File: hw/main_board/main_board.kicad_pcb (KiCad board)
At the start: 8 copper layers, 100 x 100 mm, 392 parts, among them J1 DDR2_SDRAM_SODIMM, J2 SAMTEC_QTH-090-D, J3 GSG-USB-MICRO-B-SHIELD, J4 CONN_5X2, J5 USB3_MICRO_AB, J6 HIROSE_DM3D, J7 BARREL_JACK, P1 CONN_1, P2 CONN_5X2, P3 CONN_1, Q1 BC857, SW1 SW_PUSH, U1 EP4CE30F29, U10 MIC5207YM5, U11 TPS54218, U12 TPS62420, U13 TPS27081A, U14 MIC5207YM5, U15 TPS27081A, U16 TPS27081A, U17 TPS27081A, U18 74LVC2T45, U19 GSG-IP4220CZ6, U2 TUSB1310A, U20 INV1, U3 LPC11U1X, U4 SI5351C-B, U5 GSG-IP4220CZ6, U6 MIC5207YM5, U7 USB3_ESD_SON50-10, U8 TPS2113A, U9 TPS2065C-2, X1 40M, X2 12M, X3 25M

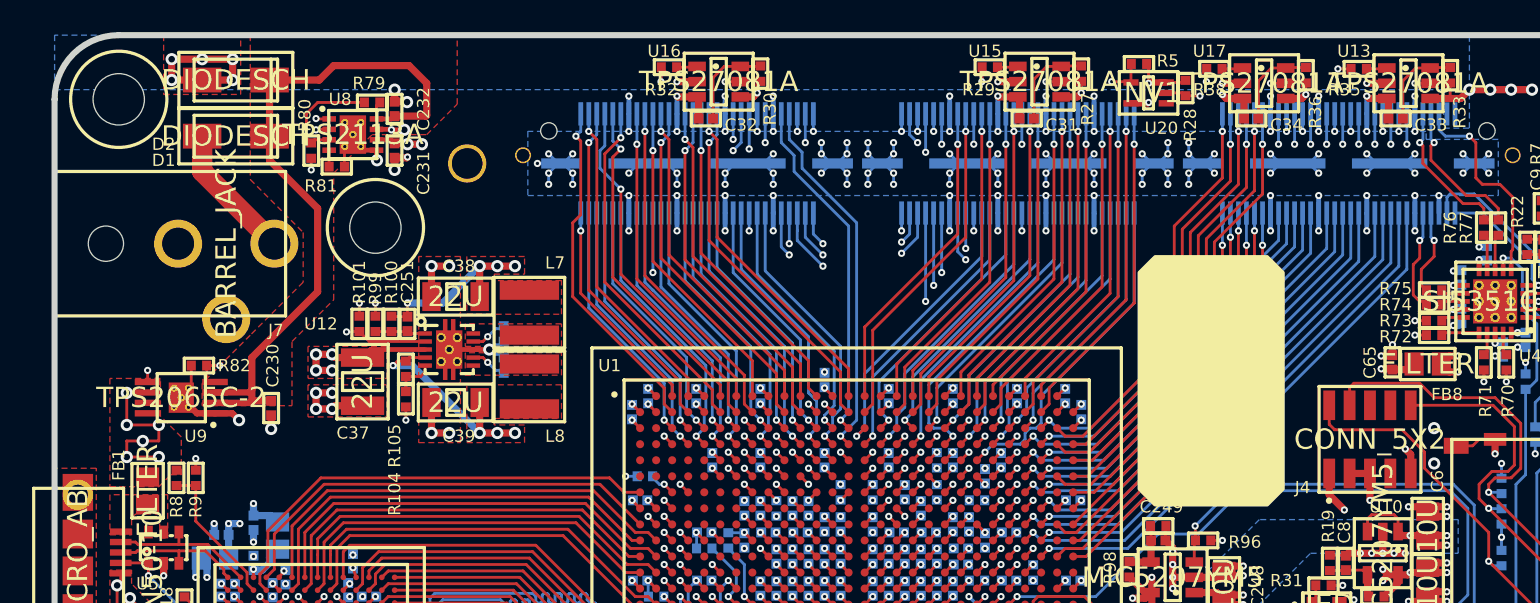
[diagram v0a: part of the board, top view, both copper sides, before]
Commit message: detect front-end module presence by VALT_FE for switching off mainboard IO bank supplies
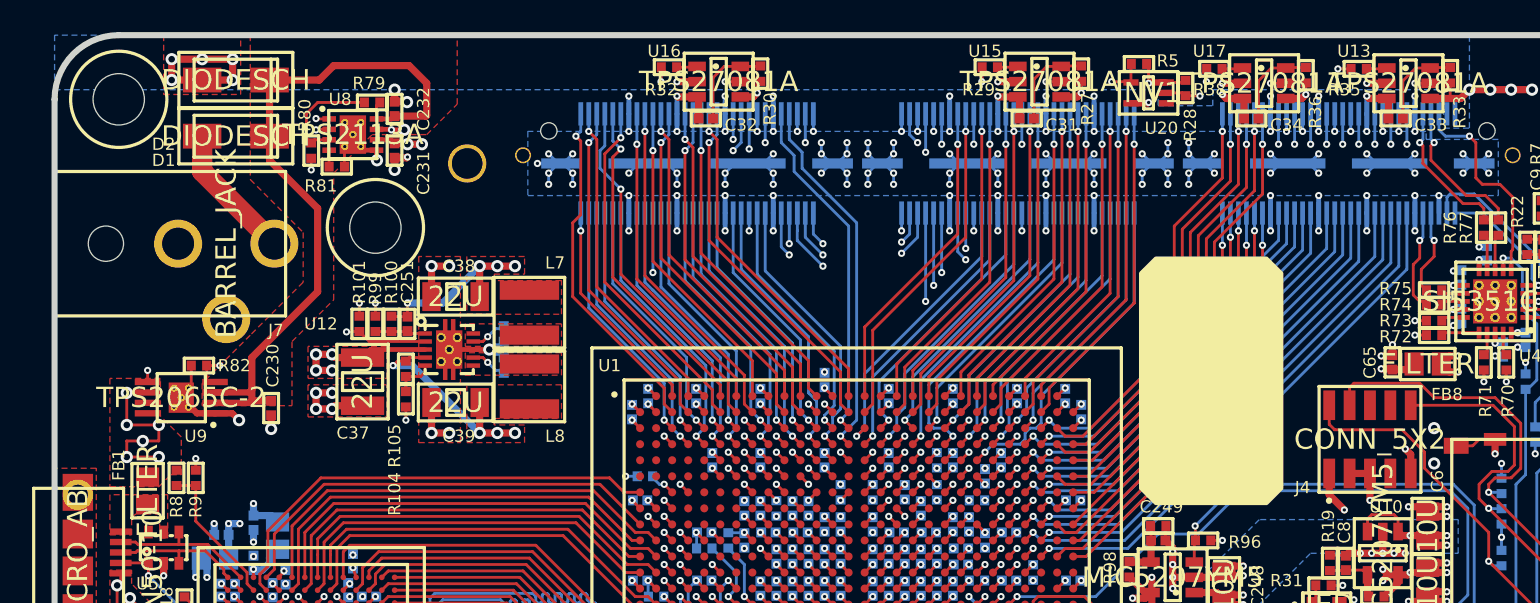
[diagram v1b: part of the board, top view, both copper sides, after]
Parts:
- C8, C9: value 470P -> DNI
- R28: value 10K -> 24K
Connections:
- J1 pad 120: (no net) -> Net-(J1-Pad120)
- J1 pad 163: (no net) -> Net-(J1-Pad163)
- J1 pad 69: (no net) -> Net-(J1-Pad69)
- J1 pad 83: (no net) -> Net-(J1-Pad83)
- J3 pad 4: (no net) -> Net-(J3-Pad4)
- J4 pad 6: (no net) -> Net-(J4-Pad6)
- J4 pad 7: (no net) -> Net-(J4-Pad7)
- J4 pad 8: (no net) -> Net-(J4-Pad8)
- J7 pad 3: (no net) -> Net-(J7-Pad3)
- P2 pad 6: (no net) -> Net-(P2-Pad6)
- P2 pad 7: (no net) -> Net-(P2-Pad7)
- P2 pad 8: (no net) -> Net-(P2-Pad8)
- R28 pad 1: /front_end/FE_EN -> VALT_FE
- U1 pad AA10: (no net) -> Net-(U1-PadAA10)
- U1 pad AA13: (no net) -> Net-(U1-PadAA13)
- U1 pad AA16: (no net) -> Net-(U1-PadAA16)
- U1 pad AA19: (no net) -> Net-(U1-PadAA19)
- U1 pad AA21: (no net) -> Net-(U1-PadAA21)
- U1 pad AA23: (no net) -> Net-(U1-PadAA23)
- U1 pad AA25: (no net) -> Net-(U1-PadAA25)
- U1 pad AA26: (no net) -> Net-(U1-PadAA26)
- U1 pad AA4: (no net) -> Net-(U1-PadAA4)
- U1 pad AA8: (no net) -> Net-(U1-PadAA8)
- U1 pad AB12: (no net) -> Net-(U1-PadAB12)
- U1 pad AB14: (no net) -> Net-(U1-PadAB14)
- U1 pad AB18: (no net) -> Net-(U1-PadAB18)
- U1 pad AB19: (no net) -> Net-(U1-PadAB19)
- U1 pad AB21: (no net) -> Net-(U1-PadAB21)
- U1 pad AB22: (no net) -> Net-(U1-PadAB22)
- U1 pad AB25: (no net) -> Net-(U1-PadAB25)
- U1 pad AB4: (no net) -> Net-(U1-PadAB4)
- U1 pad AB7: (no net) -> Net-(U1-PadAB7)
- U1 pad AB8: (no net) -> Net-(U1-PadAB8)
- U1 pad AC12: (no net) -> Net-(U1-PadAC12)
- U1 pad AC19: (no net) -> Net-(U1-PadAC19)
- U1 pad AC21: (no net) -> Net-(U1-PadAC21)
- U1 pad AC22: (no net) -> Net-(U1-PadAC22)
- U1 pad AC24: (no net) -> Net-(U1-PadAC24)
- U1 pad AC25: (no net) -> Net-(U1-PadAC25)
- U1 pad AC26: (no net) -> Net-(U1-PadAC26)
- U1 pad AD21: (no net) -> Net-(U1-PadAD21)
- U1 pad AD24: (no net) -> Net-(U1-PadAD24)
- U1 pad AD25: (no net) -> Net-(U1-PadAD25)
- U1 pad AE23: (no net) -> Net-(U1-PadAE23)
- U1 pad AE26: (no net) -> Net-(U1-PadAE26)
- U1 pad AE27: (no net) -> Net-(U1-PadAE27)
- U1 pad AG15: (no net) -> Net-(U1-PadAG15)
- U1 pad AG25: (no net) -> Net-(U1-PadAG25)
- U1 pad AH15: (no net) -> Net-(U1-PadAH15)
- U1 pad AH26: (no net) -> Net-(U1-PadAH26)
- U1 pad C17: (no net) -> Net-(U1-PadC17)
- U1 pad C2: (no net) -> Net-(U1-PadC2)
- U1 pad D1: (no net) -> Net-(U1-PadD1)
- U1 pad D2: (no net) -> Net-(U1-PadD2)
- U1 pad E1: (no net) -> Net-(U1-PadE1)
- U1 pad E2: (no net) -> Net-(U1-PadE2)
- U1 pad E27: (no net) -> Net-(U1-PadE27)
- U1 pad E3: (no net) -> Net-(U1-PadE3)
- U1 pad E4: (no net) -> Net-(U1-PadE4)
- U1 pad E5: (no net) -> Net-(U1-PadE5)
- U1 pad F1: (no net) -> Net-(U1-PadF1)
- U1 pad F14: (no net) -> Net-(U1-PadF14)
- U1 pad F2: (no net) -> Net-(U1-PadF2)
- U1 pad F3: (no net) -> Net-(U1-PadF3)
- U1 pad F4: (no net) -> Net-(U1-PadF4)
- U1 pad F5: (no net) -> Net-(U1-PadF5)
- U1 pad G11: (no net) -> Net-(U1-PadG11)
- U1 pad G13: (no net) -> Net-(U1-PadG13)
- U1 pad G19: (no net) -> Net-(U1-PadG19)
- U1 pad G2: (no net) -> Net-(U1-PadG2)
- U1 pad G22: (no net) -> Net-(U1-PadG22)
- U1 pad G27: (no net) -> Net-(U1-PadG27)
- U1 pad G5: (no net) -> Net-(U1-PadG5)
- U1 pad G6: (no net) -> Net-(U1-PadG6)
- U1 pad G7: (no net) -> Net-(U1-PadG7)
- U1 pad H10: (no net) -> Net-(U1-PadH10)
- U1 pad H12: (no net) -> Net-(U1-PadH12)
- U1 pad H13: (no net) -> Net-(U1-PadH13)
- U1 pad H14: (no net) -> Net-(U1-PadH14)
- U1 pad H15: (no net) -> Net-(U1-PadH15)
- U1 pad H19: (no net) -> Net-(U1-PadH19)
- U1 pad H21: (no net) -> Net-(U1-PadH21)
- U1 pad H22: (no net) -> Net-(U1-PadH22)
- U1 pad H4: (no net) -> Net-(U1-PadH4)
- U1 pad H5: (no net) -> Net-(U1-PadH5)
- U1 pad H6: (no net) -> Net-(U1-PadH6)
- U1 pad H7: (no net) -> Net-(U1-PadH7)
- U1 pad H8: (no net) -> Net-(U1-PadH8)
- U1 pad J10: (no net) -> Net-(U1-PadJ10)
- U1 pad J12: (no net) -> Net-(U1-PadJ12)
- U1 pad J14: (no net) -> Net-(U1-PadJ14)
- U1 pad J16: (no net) -> Net-(U1-PadJ16)
- U1 pad J19: (no net) -> Net-(U1-PadJ19)
- U1 pad J4: (no net) -> Net-(U1-PadJ4)
- U1 pad J5: (no net) -> Net-(U1-PadJ5)
- U1 pad J6: (no net) -> Net-(U1-PadJ6)
- U1 pad J7: (no net) -> Net-(U1-PadJ7)
- U1 pad K13: (no net) -> Net-(U1-PadK13)
- U1 pad K15: (no net) -> Net-(U1-PadK15)
- U1 pad K21: (no net) -> Net-(U1-PadK21)
- U1 pad K22: (no net) -> Net-(U1-PadK22)
- U1 pad K27: (no net) -> Net-(U1-PadK27)
- U1 pad K7: (no net) -> Net-(U1-PadK7)
- U1 pad L20: (no net) -> Net-(U1-PadL20)
- U1 pad L22: (no net) -> Net-(U1-PadL22)
- U1 pad L5: (no net) -> Net-(U1-PadL5)
- U1 pad L6: (no net) -> Net-(U1-PadL6)
- U1 pad L7: (no net) -> Net-(U1-PadL7)
- U1 pad L8: (no net) -> Net-(U1-PadL8)
- U1 pad M26: (no net) -> Net-(U1-PadM26)
- U1 pad M27: (no net) -> Net-(U1-PadM27)
- U1 pad M28: (no net) -> Net-(U1-PadM28)
- U1 pad M5: (no net) -> Net-(U1-PadM5)
- U1 pad M7: (no net) -> Net-(U1-PadM7)
- U1 pad M8: (no net) -> Net-(U1-PadM8)
- U1 pad M9: (no net) -> Net-(U1-PadM9)
- U1 pad N25: (no net) -> Net-(U1-PadN25)
- U1 pad N26: (no net) -> Net-(U1-PadN26)
- U1 pad N8: (no net) -> Net-(U1-PadN8)
- U1 pad P21: (no net) -> Net-(U1-PadP21)
- U1 pad P25: (no net) -> Net-(U1-PadP25)
- U1 pad P26: (no net) -> Net-(U1-PadP26)
- U1 pad P27: (no net) -> Net-(U1-PadP27)
- U1 pad P28: (no net) -> Net-(U1-PadP28)
- U1 pad R21: (no net) -> Net-(U1-PadR21)
- U1 pad R22: (no net) -> Net-(U1-PadR22)
- U1 pad R23: (no net) -> Net-(U1-PadR23)
- U1 pad T21: (no net) -> Net-(U1-PadT21)
- U1 pad T22: (no net) -> Net-(U1-PadT22)
- U1 pad T26: (no net) -> Net-(U1-PadT26)
- U1 pad T7: (no net) -> Net-(U1-PadT7)
- U1 pad T8: (no net) -> Net-(U1-PadT8)
- U1 pad T9: (no net) -> Net-(U1-PadT9)
- U1 pad U20: (no net) -> Net-(U1-PadU20)
- U1 pad U22: (no net) -> Net-(U1-PadU22)
- U1 pad U25: (no net) -> Net-(U1-PadU25)
- U1 pad U26: (no net) -> Net-(U1-PadU26)
- U1 pad U27: (no net) -> Net-(U1-PadU27)
- U1 pad U6: (no net) -> Net-(U1-PadU6)
- U1 pad U7: (no net) -> Net-(U1-PadU7)
- U1 pad U8: (no net) -> Net-(U1-PadU8)
- U1 pad V20: (no net) -> Net-(U1-PadV20)
- U1 pad V21: (no net) -> Net-(U1-PadV21)
- U1 pad V22: (no net) -> Net-(U1-PadV22)
- U1 pad V23: (no net) -> Net-(U1-PadV23)
- U1 pad V24: (no net) -> Net-(U1-PadV24)
- U1 pad V26: (no net) -> Net-(U1-PadV26)
- U1 pad V27: (no net) -> Net-(U1-PadV27)
- U1 pad V6: (no net) -> Net-(U1-PadV6)
- U1 pad V8: (no net) -> Net-(U1-PadV8)
- U1 pad V9: (no net) -> Net-(U1-PadV9)
- U1 pad W10: (no net) -> Net-(U1-PadW10)
- U1 pad W16: (no net) -> Net-(U1-PadW16)
- U1 pad W20: (no net) -> Net-(U1-PadW20)
- U1 pad W21: (no net) -> Net-(U1-PadW21)
- U1 pad W22: (no net) -> Net-(U1-PadW22)
- U1 pad W25: (no net) -> Net-(U1-PadW25)
- U1 pad W8: (no net) -> Net-(U1-PadW8)
- U1 pad W9: (no net) -> Net-(U1-PadW9)
- U1 pad Y1: (no net) -> Net-(U1-PadY1)
- U1 pad Y12: (no net) -> Net-(U1-PadY12)
- U1 pad Y13: (no net) -> Net-(U1-PadY13)
- U1 pad Y14: (no net) -> Net-(U1-PadY14)
- U1 pad Y15: (no net) -> Net-(U1-PadY15)
- U1 pad Y19: (no net) -> Net-(U1-PadY19)
- U1 pad Y22: (no net) -> Net-(U1-PadY22)
- U1 pad Y23: (no net) -> Net-(U1-PadY23)
- U1 pad Y25: (no net) -> Net-(U1-PadY25)
- U1 pad Y5: (no net) -> Net-(U1-PadY5)
- U1 pad Y7: (no net) -> Net-(U1-PadY7)
- U19 pad 4: (no net) -> Net-(U19-Pad4)
- U19 pad 6: (no net) -> Net-(U19-Pad6)
- U2 pad A14: (no net) -> Net-(U2-PadA14)
- U2 pad C13: (no net) -> Net-(U2-PadC13)
- U2 pad C14: (no net) -> Net-(U2-PadC14)
- U2 pad D10: (no net) -> Net-(U2-PadD10)
- U2 pad D11: (no net) -> Net-(U2-PadD11)
- U2 pad D5: (no net) -> Net-(U2-PadD5)
- U2 pad D6: (no net) -> Net-(U2-PadD6)
- U2 pad E11: (no net) -> Net-(U2-PadE11)
- U2 pad E12: (no net) -> Net-(U2-PadE12)
- U2 pad F11: (no net) -> Net-(U2-PadF11)
- U2 pad G11: (no net) -> Net-(U2-PadG11)
- U2 pad H12: (no net) -> Net-(U2-PadH12)
- U2 pad J12: (no net) -> Net-(U2-PadJ12)
- U2 pad J4: (no net) -> Net-(U2-PadJ4)
- U2 pad K4: (no net) -> Net-(U2-PadK4)
- U20 pad 2: /front_end/FE_EN -> VALT_FE
- U5 pad 6: (no net) -> Net-(U5-Pad6)
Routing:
- net /front_end/FE_EN: track 76.8 -> 60.4 mm, vias 3 -> 2
- net VALT_FE: track 10.2 -> 12.4 mm, vias 5 -> 6

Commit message: mainboard: layer legend
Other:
- board text added: "1"
- board text added: "2"
- board text added: "3"
- board text added: "4"
- board text added: "5"
- board text added: "6"
- board text added: "7"
- board text added: "8"

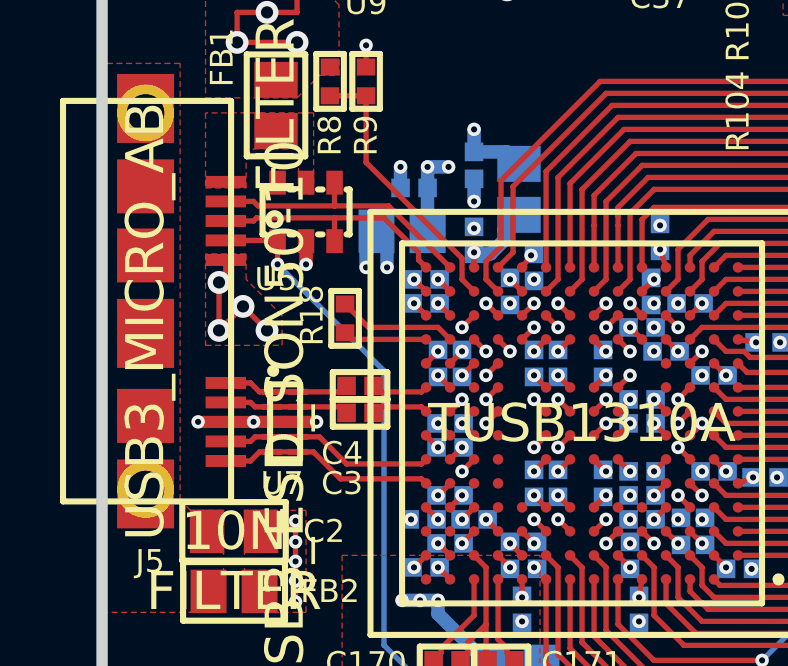
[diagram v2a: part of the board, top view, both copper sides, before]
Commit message: mainboard: improved USB differential trace impedance
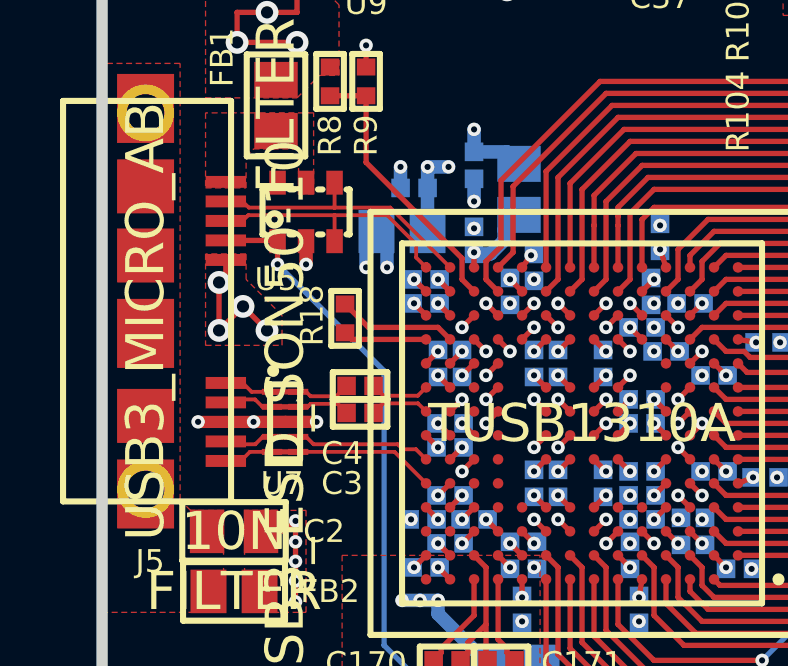
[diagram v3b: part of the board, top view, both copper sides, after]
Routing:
- net /usb0_interfaces/SSTXM_C: track 4.23 -> 5.50 mm
- net /usb0_interfaces/SSRXP: track 7.23 -> 8.41 mm
- net /usb0_interfaces/SSRXM: track 7.17 -> 8.13 mm
- net /usb0_interfaces/SSTXP_C: track 4.17 -> 5.11 mm
- net /usb0_interfaces/DM: track 9.16 -> 10.1 mm
- net /usb0_interfaces/DP: track 8.33 -> 9.06 mm
- net /usb0_interfaces/SSTXP: track 1.89 -> 2.42 mm
- net /usb0_interfaces/SSTXM: track 1.90 -> 2.41 mm
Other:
- net class 45 Ohm: trace_width 0.1651 -> 0.127
- rule trace_min: 0.1651 -> 0.127
